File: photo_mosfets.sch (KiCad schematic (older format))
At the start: 30 parts, among them U10 TLP3543, U11 TLP3543, U12 TLP3543, U3 TLP3543, U4 TLP3543, U5 TLP3543, U6 TLP3543, U7 TLP3543, U8 TLP3543, U9 TLP3543

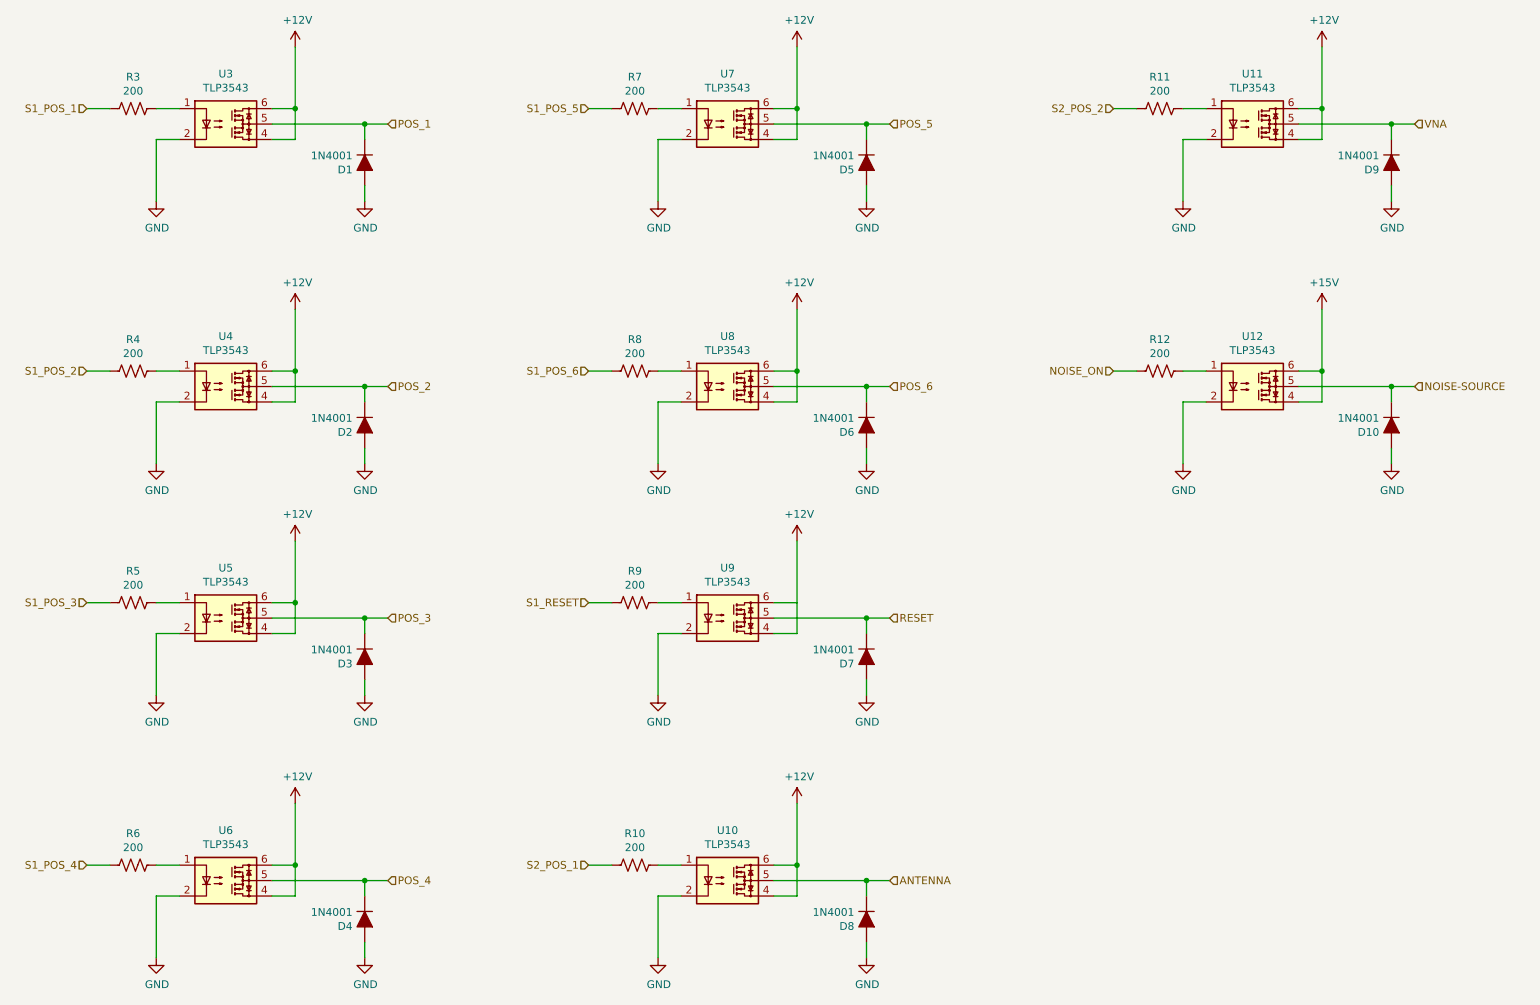
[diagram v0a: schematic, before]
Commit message: Added MFN, MPN, VN and VPN fields for all symbols
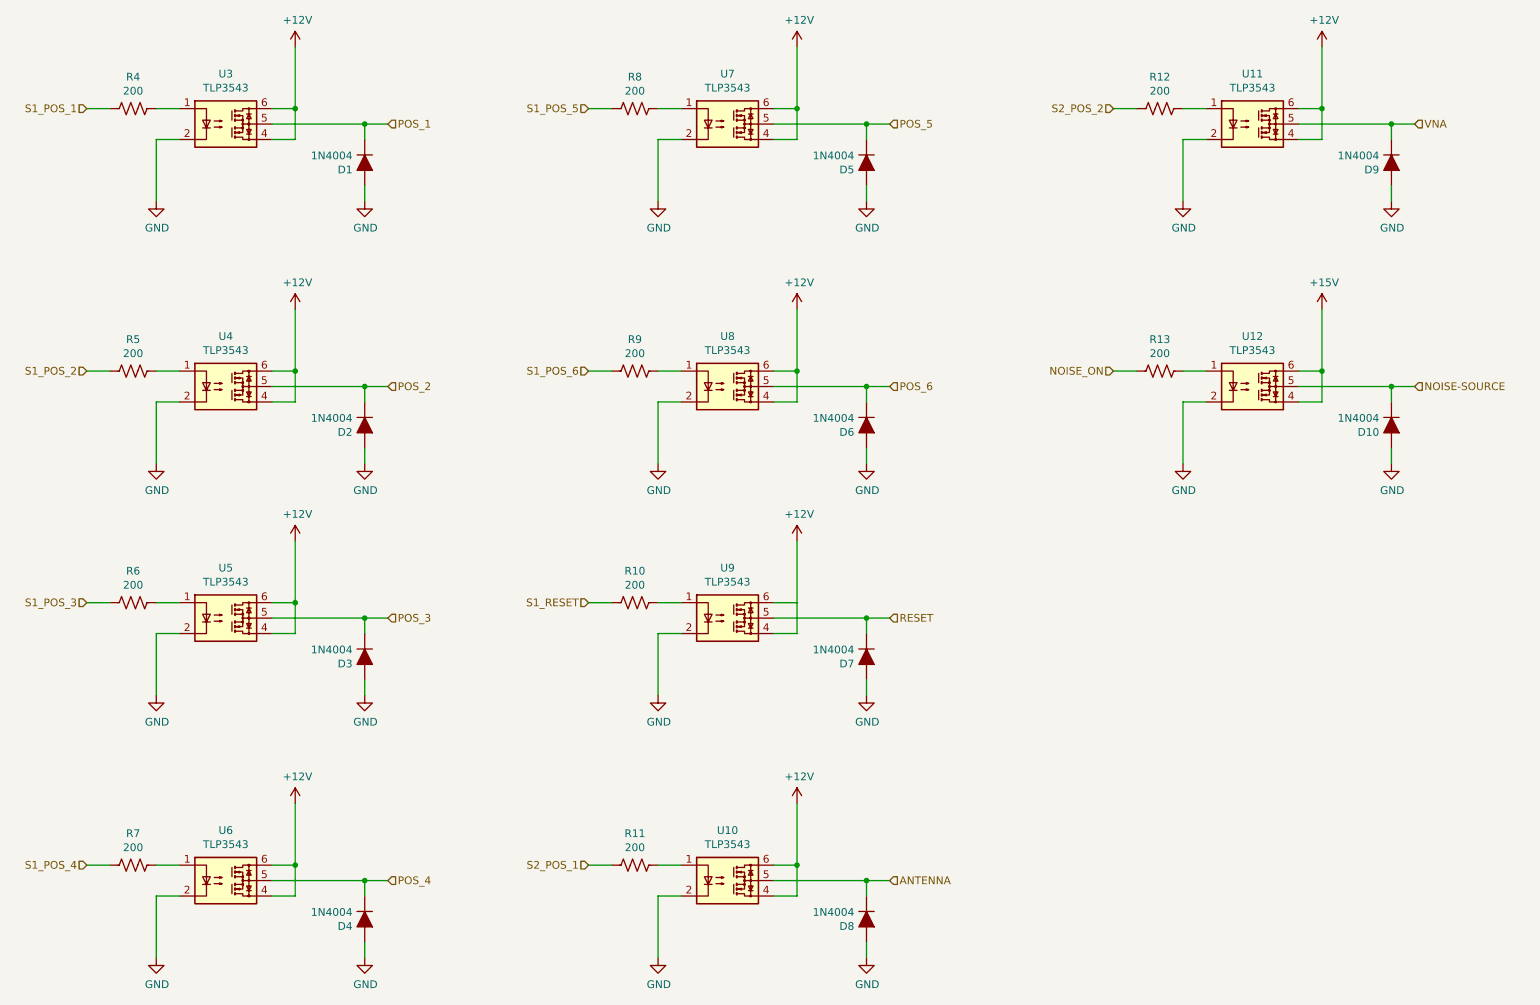
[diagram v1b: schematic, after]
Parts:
- D1, D10, D2, D3, D4, D5, D6, D7, D8, D9: value 1N4001 -> 1N4004; MFN (none) -> Generic; MPN (none) -> Generic; VN (none) -> Digikey; VPN (none) -> 1N4004-TPMSCT-ND
- R10: renamed from R9; MFN (none) -> Generic; MPN (none) -> Generic; VN (none) -> Digikey; VPN (none) -> P200HCT-ND
- R11: renamed from R10; MFN (none) -> Generic; MPN (none) -> Generic; VN (none) -> Digikey; VPN (none) -> P200HCT-ND
- R12: renamed from R11; MFN (none) -> Generic; MPN (none) -> Generic; VN (none) -> Digikey; VPN (none) -> P200HCT-ND
- R13: renamed from R12; MFN (none) -> Generic; MPN (none) -> Generic; VN (none) -> Digikey; VPN (none) -> P200HCT-ND
- R4: renamed from R3; MFN (none) -> Generic; MPN (none) -> Generic; VN (none) -> Digikey; VPN (none) -> P200HCT-ND
- R5: renamed from R4; MFN (none) -> Generic; MPN (none) -> Generic; VN (none) -> Digikey; VPN (none) -> P200HCT-ND
- R6: renamed from R5; MFN (none) -> Generic; MPN (none) -> Generic; VN (none) -> Digikey; VPN (none) -> P200HCT-ND
- R7: renamed from R6; MFN (none) -> Generic; MPN (none) -> Generic; VN (none) -> Digikey; VPN (none) -> P200HCT-ND
- R8: renamed from R7; MFN (none) -> Generic; MPN (none) -> Generic; VN (none) -> Digikey; VPN (none) -> P200HCT-ND
- R9: renamed from R8; MFN (none) -> Generic; MPN (none) -> Generic; VN (none) -> Digikey; VPN (none) -> P200HCT-ND
- U10, U11, U12, U3, U4, U5, U6, U7, U8, U9: MFN (none) -> Toshiba Semiconductor and Storage; MPN (none) -> TLP3543(F); VN (none) -> Digikey; VPN (none) -> TLP3543(F)-ND
